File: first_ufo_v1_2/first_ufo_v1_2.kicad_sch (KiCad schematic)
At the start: 71 parts, among them J2 Barrel_Jack_Switch, Q1 2N3904, SW1 SMTS-102, SW2 SMTS-102, SW3 SMTS-102, U1 40106, U3 LM358

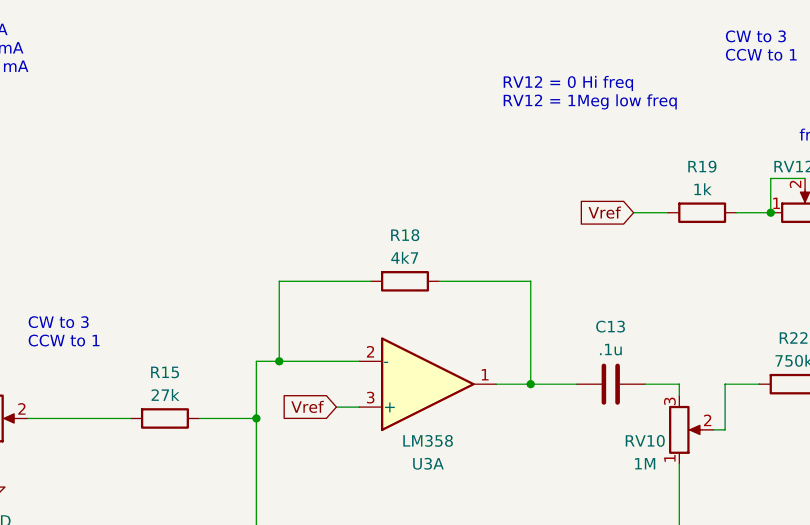
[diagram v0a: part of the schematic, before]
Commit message: changed R18 to 1k for better dynamic range in case of high volume level of three oscs added verison title on pcb
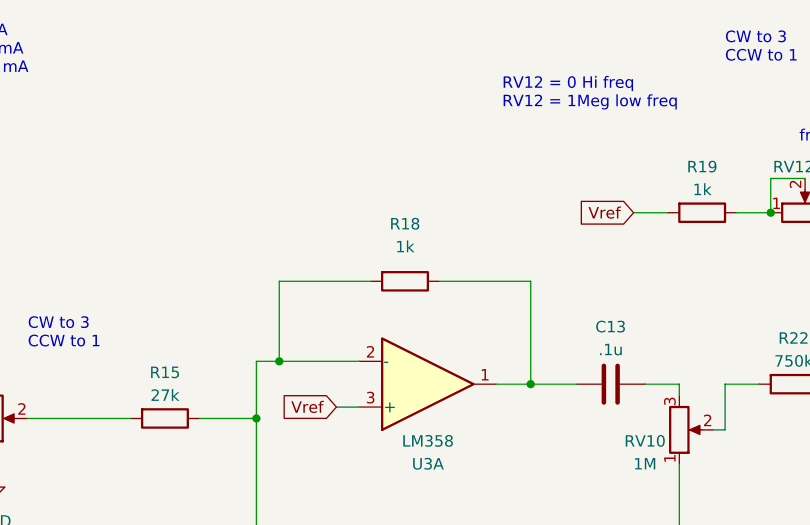
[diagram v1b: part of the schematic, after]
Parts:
- D5: footprint Import:tactile pad triangle -> Import:tactile pad triangle_1
- R18: value 4k7 -> 1k
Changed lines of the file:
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@@
 			)
 		)
-		(property "Footprint" "Import:tactile pad triangle"
+		(property "Footprint" "Import:tactile pad triangle_1"
 			(at 107.95 67.31 0)
 			(effects
@@
 		(fields_autoplaced yes)
 		(property "Reference" "R18"
-			(at 186.69 38.1 90)
+			(at 186.69 36.83 90)
 			(effects
 				(font
@@
 			)
 		)
-		(property "Value" "4k7"
-			(at 186.69 40.64 90)
+		(property "Value" "1k"
+			(at 186.69 39.37 90)
 			(effects
 				(font
